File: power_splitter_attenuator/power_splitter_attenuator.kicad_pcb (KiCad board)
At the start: 4 copper layers, 46.2 x 46.2 mm, 40 parts, among them J1 SMA, J2 SMA, J3 SMA, J4 SMA, J5 SMA, J6 SMA, J7 SMA, J8 SMA

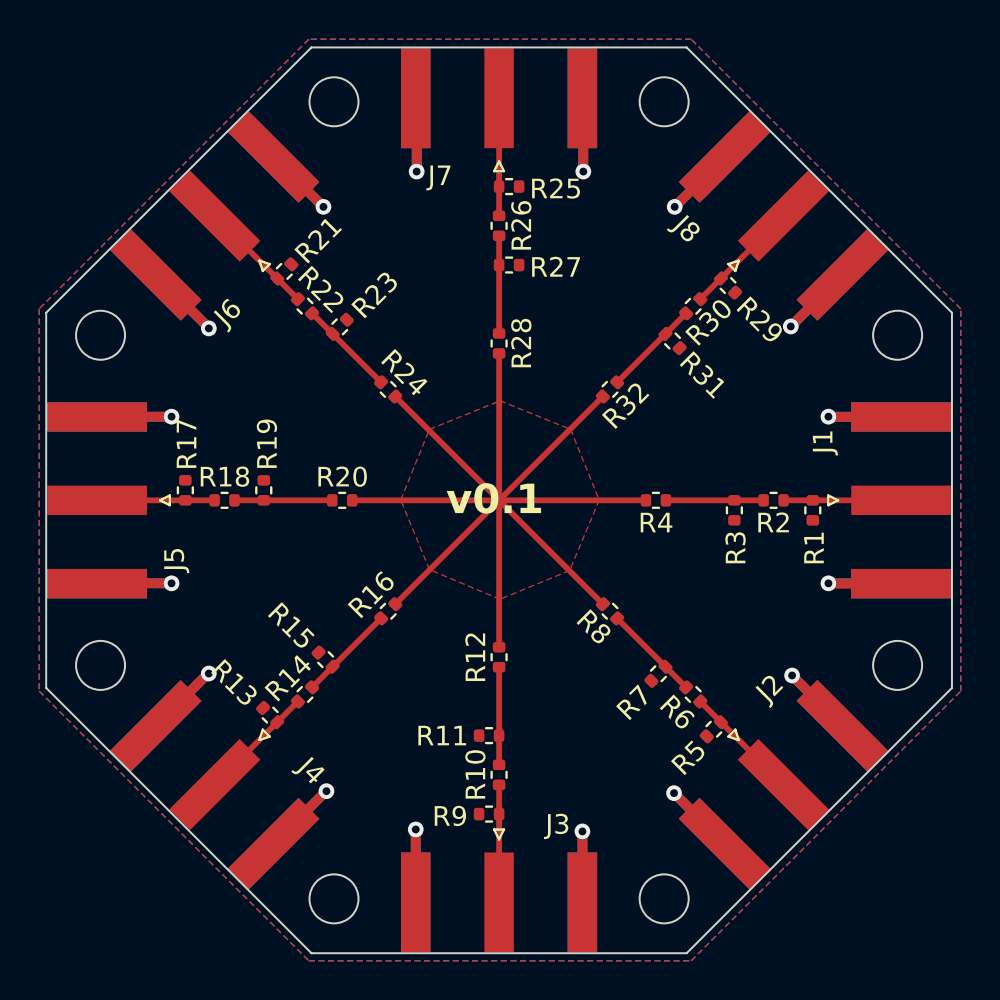
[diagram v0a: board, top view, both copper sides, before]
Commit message: power splitter: implement feedback from review
- smaller octagon in center
- copper fill keepout zone below SMA center pad
- copper fill keepout zone around holes (1.5mm radius)
- increase hole radius from 1.25mm to 1.3mm
- add lots of GND vias
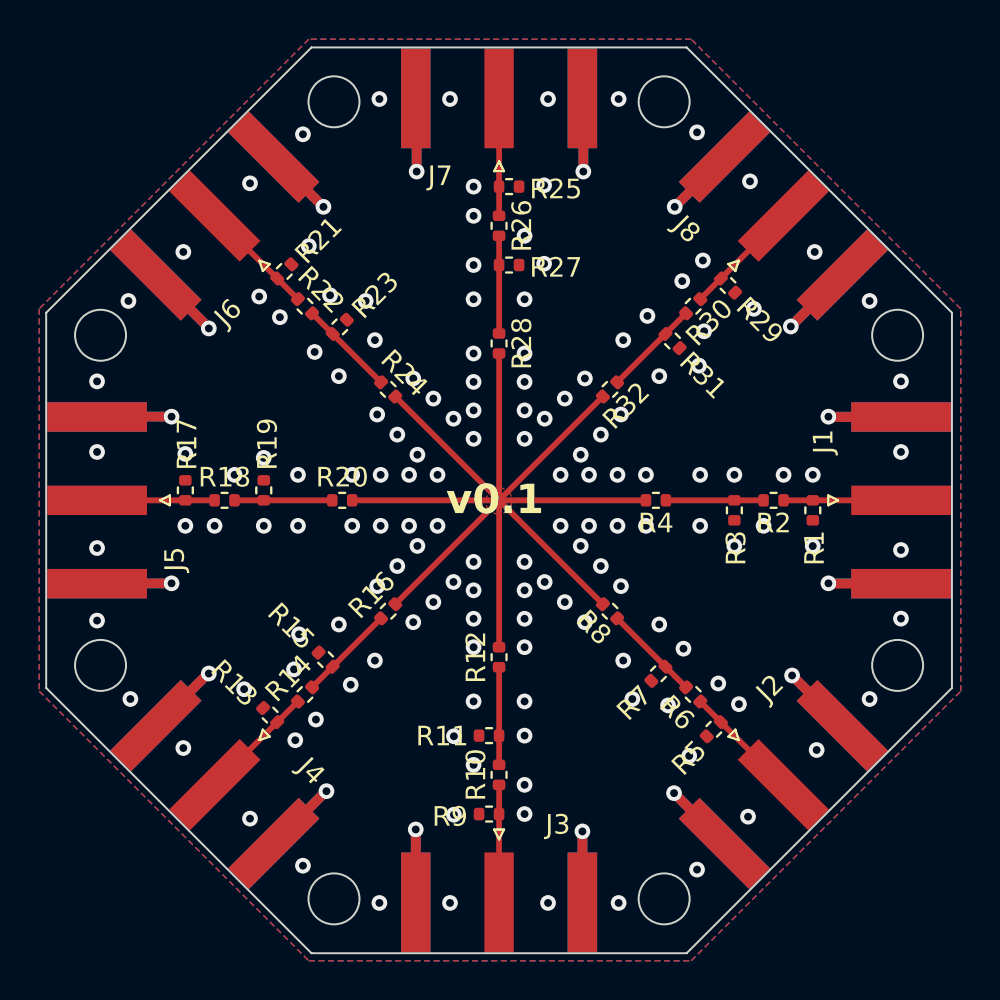
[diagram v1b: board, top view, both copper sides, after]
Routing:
- net GND: vias 16 -> 168
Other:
- outline, holes or cut-outs redrawn
